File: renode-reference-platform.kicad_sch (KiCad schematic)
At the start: 28 parts

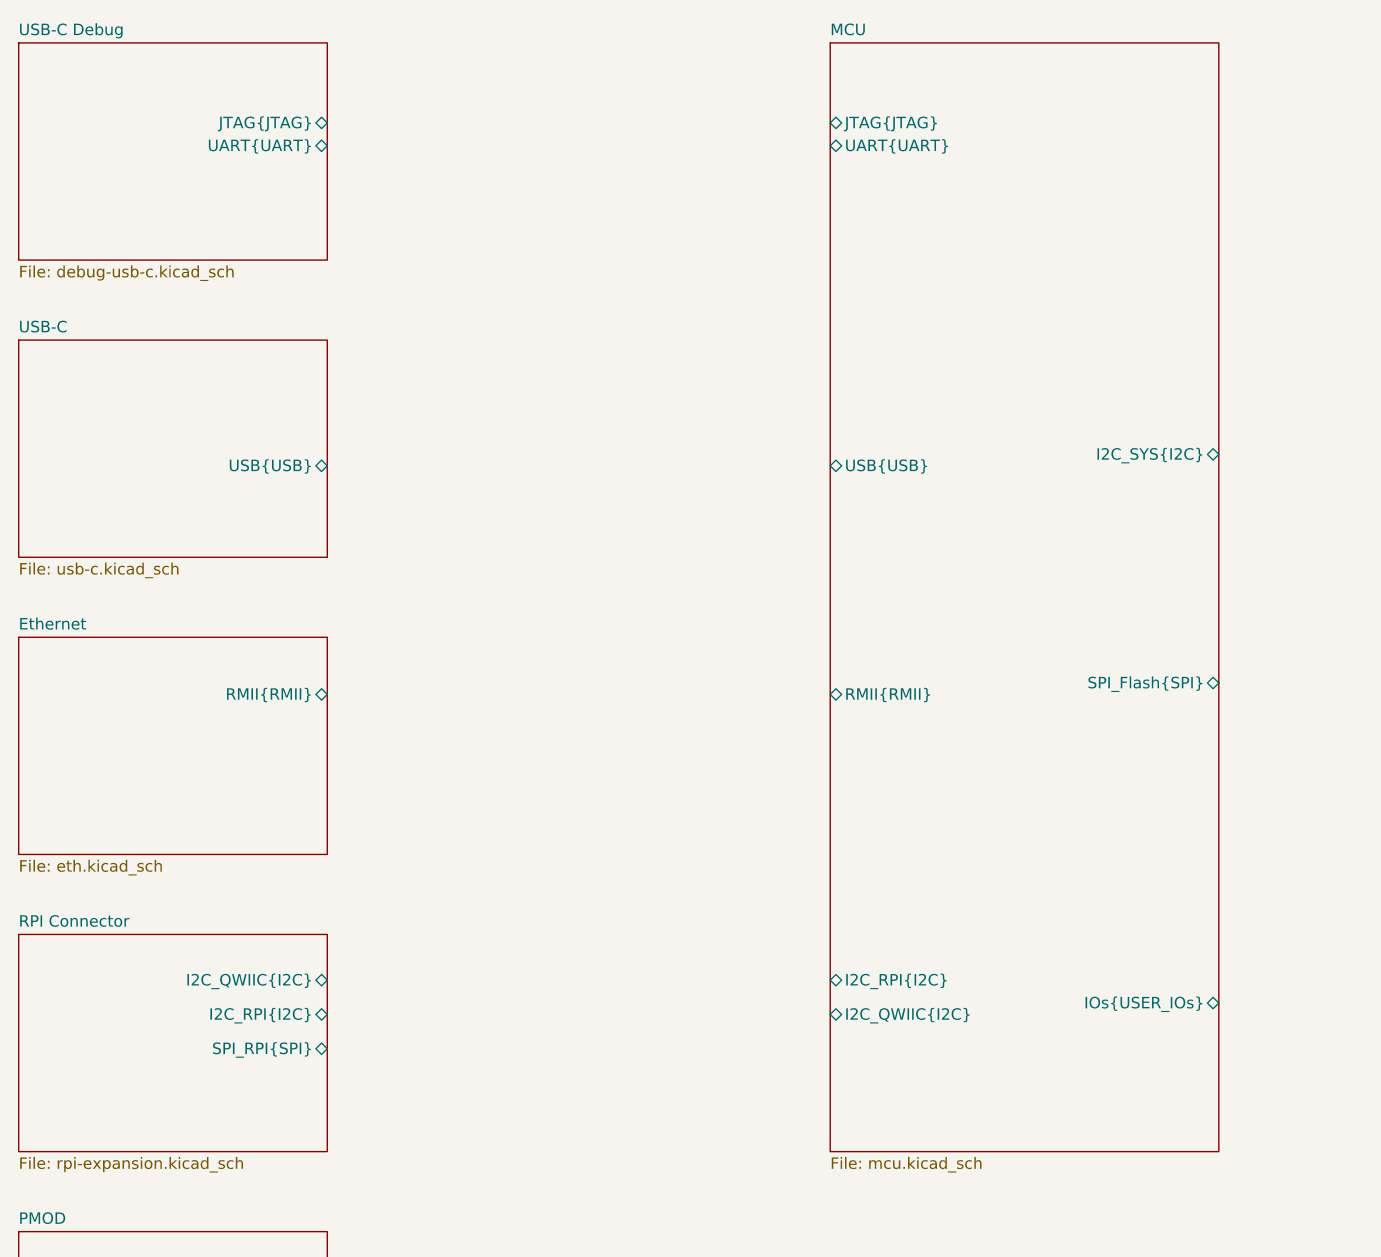
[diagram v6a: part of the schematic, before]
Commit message: [94727] Reconnect buses to MCU to sovle overlaping signals
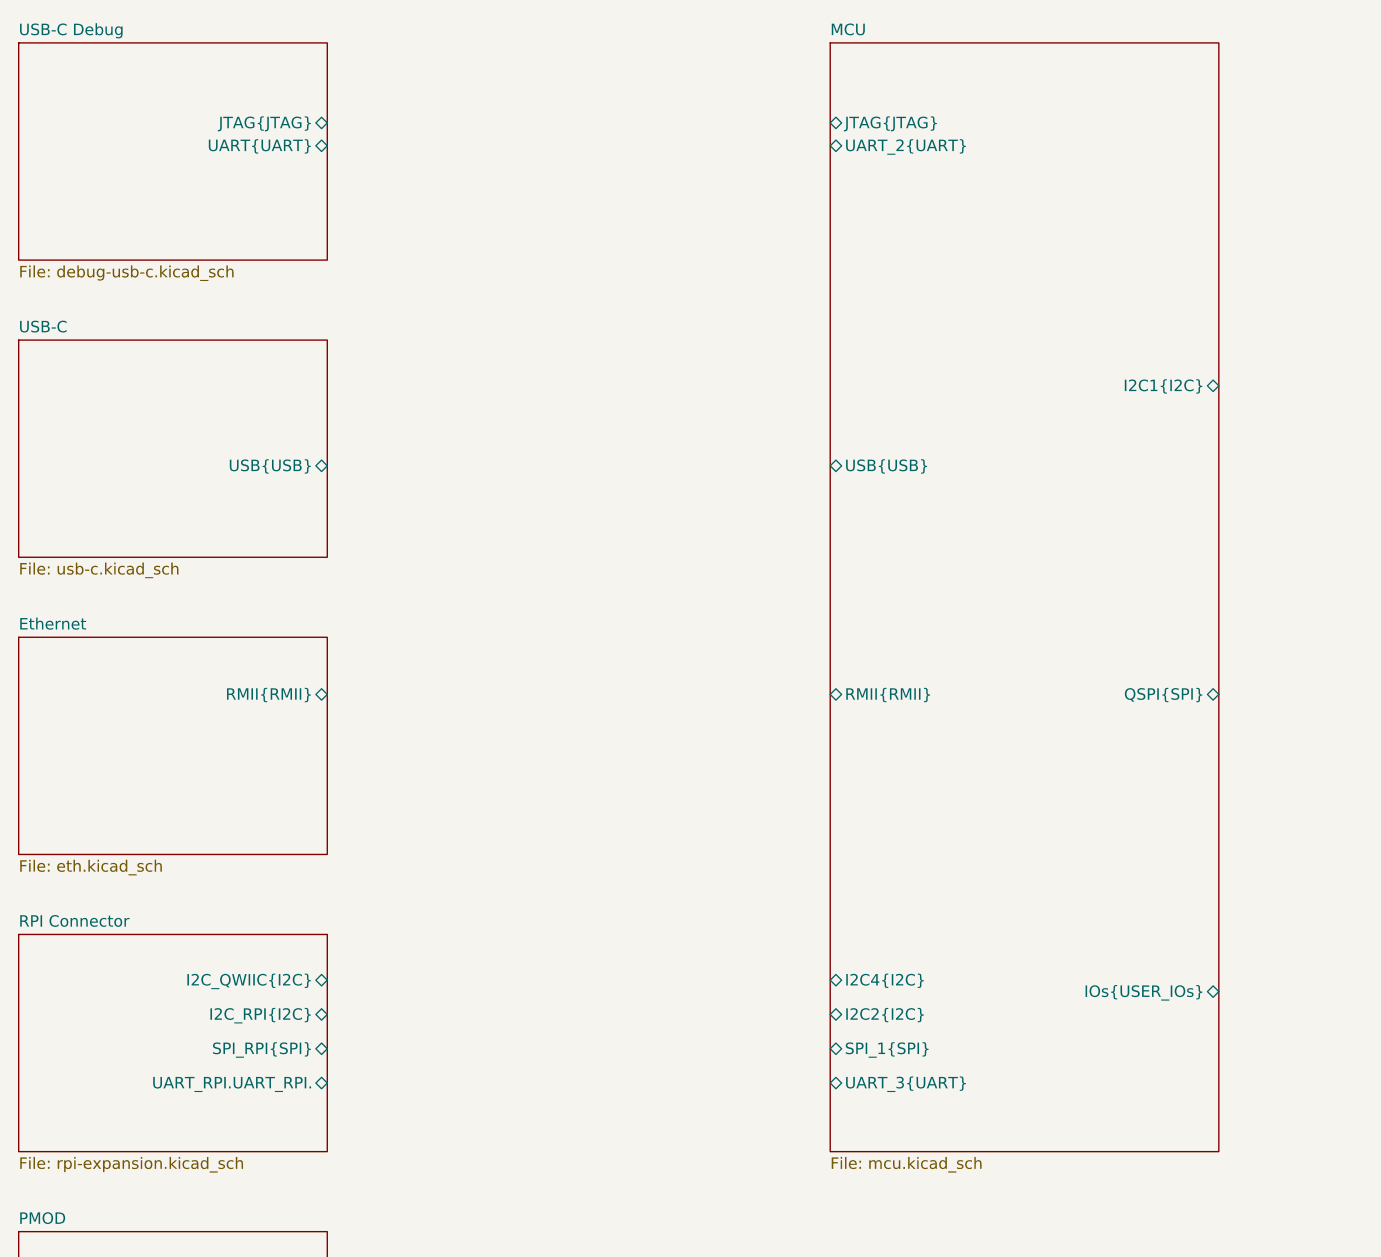
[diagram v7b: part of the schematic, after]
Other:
- sheet MCU ports: added I2C1{I2C}, I2C2{I2C}, I2C4{I2C}, QSPI{SPI}, SPI_1{SPI}, UART_2{UART}, UART_3{UART}; removed I2C_QWIIC{I2C}, I2C_RPI{I2C}, I2C_SYS{I2C}, SPI_Flash{SPI}, UART{UART}
- sheet RPI Connector ports: added UART_RPI.UART_RPI.; removed none
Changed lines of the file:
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@@
 	)
 	(bus_alias "USB"
-		(members "D+" "D-")
+		(members "D+" "D-" "ID" "VBUS")
 	)
 	(image
@@
 			)
 		)
+		(pin "UART_RPI.UART_RPI." bidirectional
+			(at 99.06 200.66 0)
+			(effects
+				(font
+					(size 1.27 1.27)
+				)
+				(justify right)
+			)
+		)
 		(instances
 			(project "renode-reference-platform"
@@
 			)
 		)
-		(pin "RMII{RMII}" bidirectional
-			(at 154.94 157.48 180)
+		(pin "I2C1{I2C}" bidirectional
+			(at 198.12 123.19 0)
+			(effects
+				(font
+					(size 1.27 1.27)
+				)
+				(justify right)
+			)
+		)
+		(pin "I2C2{I2C}" bidirectional
+			(at 154.94 193.04 180)
 			(effects
 				(font
@@
 			)
 		)
-		(pin "I2C_SYS{I2C}" bidirectional
-			(at 198.12 130.81 0)
+		(pin "I2C4{I2C}" bidirectional
+			(at 154.94 189.23 180)
 			(effects
 				(font
 					(size 1.27 1.27)
 				)
-				(justify right)
+				(justify left)
 			)
 		)
-		(pin "SPI_Flash{SPI}" bidirectional
-			(at 198.12 156.21 0)
+		(pin "IOs{USER_IOs}" bidirectional
+			(at 198.12 190.5 0)
 			(effects
 				(font
@@
 			)
 		)
-		(pin "IOs{USER_IOs}" bidirectional
-			(at 198.12 191.77 0)
+		(pin "JTAG{JTAG}" bidirectional
+			(at 154.94 93.98 180)
+			(effects
+				(font
+					(size 1.27 1.27)
+				)
+				(justify left)
+			)
+		)
+		(pin "QSPI{SPI}" bidirectional
+			(at 198.12 157.48 0)
 			(effects
 				(font
@@
 			)
 		)
-		(pin "USB{USB}" bidirectional
-			(at 154.94 132.08 180)
+		(pin "RMII{RMII}" bidirectional
+			(at 154.94 157.48 180)
 			(effects
 				(font
@@
 			)
 		)
-		(pin "JTAG{JTAG}" bidirectional
-			(at 154.94 93.98 180)
+		(pin "SPI_1{SPI}" bidirectional
+			(at 154.94 196.85 180)
 			(effects
 				(font
@@
 			)
 		)
-		(pin "UART{UART}" bidirectional
+		(pin "UART_2{UART}" bidirectional
 			(at 154.94 96.52 180)
 			(effects
@@
 			)
 		)
-		(pin "I2C_RPI{I2C}" bidirectional
-			(at 154.94 189.23 180)
+		(pin "UART_3{UART}" bidirectional
+			(at 154.94 200.66 180)
 			(effects
 				(font
@@
 			)
 		)
-		(pin "I2C_QWIIC{I2C}" bidirectional
-			(at 154.94 193.04 180)
+		(pin "USB{USB}" bidirectional
+			(at 154.94 132.08 180)
 			(effects
 				(font

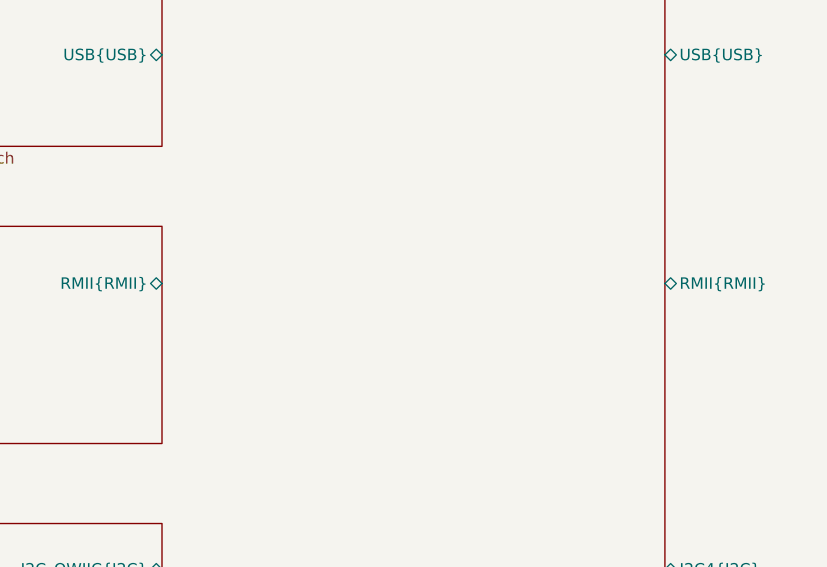
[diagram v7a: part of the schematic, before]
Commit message: [#94823] Add RMII termination
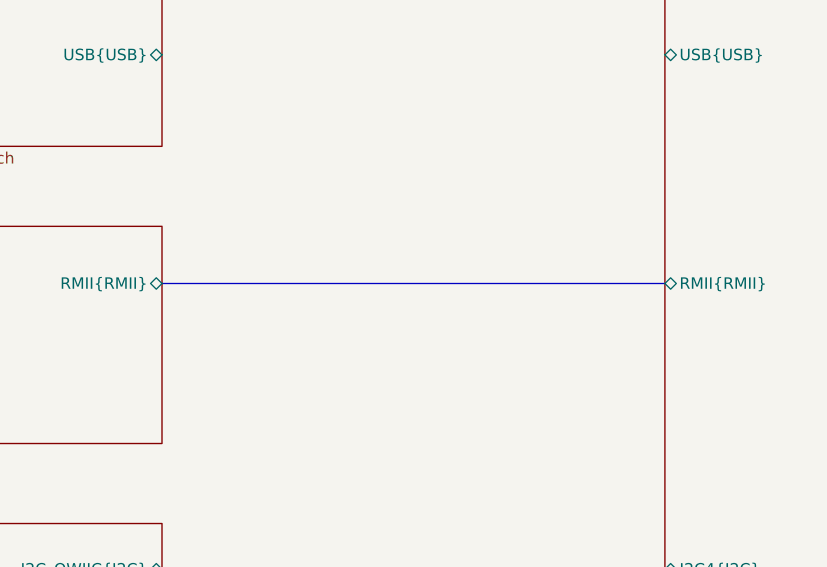
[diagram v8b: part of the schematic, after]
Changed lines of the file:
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@@
 		(members "D+" "D-" "ID" "VBUS")
+	)
+	(bus
+		(pts
+			(xy 99.06 157.48) (xy 154.94 157.48)
+		)
+		(stroke
+			(width 0)
+			(type default)
+		)
 	)
 	(image
